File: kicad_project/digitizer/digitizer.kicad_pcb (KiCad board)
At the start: 2 copper layers, 96 x 74 mm, 63 parts, among them IC201 MAX3059ASA+T UPSTREAM, IC202 MAX6035AAUR50+T, IC203 MAX3059ASA+T DOWNSTREAM, IC204 MAX6043BAUT33+T, IC301 ADS1234IPWR, J201 DT15-4P (UPSTREAM), J202 DT06-4S (DOWNSTREAM), J301 Load Cell 1, J302 Load Cell 2, J303 Load Cell 3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

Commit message: continued layout progress; connected JTAG connector and reset switch, among a few other changes
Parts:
- C303: moved to F.Cu
- C405, R407: moved to B.Cu
- moved R307 103.3 mm to (130.5, 104.6)
- moved R306 84.3 mm to (130.5, 102.5)
- moved R407 81.3 mm to (99.3, 81.3), turned to 90 degrees
- moved R406 74.6 mm to (107.5, 59.2)
- moved C405 66.8 mm to (102.5, 82.2)
- moved R405 62.6 mm to (103.6, 59.2), turned to 180 degrees
- moved R401 62.5 mm to (98.8, 55.0), turned to 90 degrees
- moved R402 60.8 mm to (99.7, 59.2), turned to 180 degrees
- moved J401 5.10 mm to (101.5, 54.8), turned to 0 degrees
- moved REF** 4.24 mm to (82.2, 115.0)
- moved C304 3.00 mm to (147.4, 113.5)
- moved C306 3.00 mm to (83.0, 105.3)
- moved C307 3.00 mm to (113.5, 114.0)
- moved J202 3.00 mm to (85.5, 63.8)
- moved J301 3.00 mm to (85.5, 87.7)
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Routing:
- net NRESET: track 0.00 -> 35.2 mm
- net GND: track 28.5 -> 33.8 mm, vias 3 -> 4
- net MCU_NRESET: track 0.00 -> 4.56 mm, vias 0 -> 1
- net Net-(IC301-Pad20): track 0.00 -> 4.23 mm
- net /MCU/TCLK: track 0.00 -> 4.00 mm
- net /MCU/TDI: track 0.00 -> 3.67 mm
- net Net-(IC301-Pad19): track 0.00 -> 3.63 mm
- net /ANALOG/load cell 2 - signal (-): track 12.5 -> 8.90 mm
- net /MCU/TDO: track 0.00 -> 3.41 mm
- net /ANALOG/load cell 1 - signal (-): track 41.3 -> 38.3 mm
- net /ANALOG/load cell 1 - signal (+): track 42.3 -> 39.3 mm
- net /MCU/TMS: track 0.00 -> 2.68 mm
- net Net-(C303-Pad2): track 6.68 -> 5.17 mm, vias 1 -> 0
- net /CANPWR/CANH_DOWNSTREAM: track 39.3 -> 38.0 mm
- net /ANALOG/load cell 3 - signal (-): track 29.7 -> 28.5 mm
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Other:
- board size 96 x 74 mm -> 93 x 71 mm

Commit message: more progress! CAN ICs are done, just the MCU Power decoupling is left
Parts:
- C202, C203: moved to B.Cu
- moved C202 114.0 mm to (105.2, 97.5), turned to -90 degrees
- moved C203 107.7 mm to (95.5, 97.5), turned to -90 degrees
- moved R202 2.44 mm to (99.2, 93.3)
- moved C304 2.44 mm to (149.8, 114.0)
- moved J303 2.22 mm to (132.2, 111.5)
- moved IC203 2.20 mm to (95.5, 97.5)
- moved C307 1.54 mm to (112.0, 114.0)
- moved J302 1.50 mm to (94.5, 111.5)
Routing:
- net /CANPWR/CANL_UPSTREAM: track 0.00 -> 65.3 mm, vias 0 -> 2
- net /CANPWR/CANH_UPSTREAM: track 0.00 -> 61.6 mm, vias 0 -> 1
- net CAN_DOWN_RX: track 0.00 -> 44.0 mm, vias 0 -> 2
- net CAN_DOWN_TX: track 0.00 -> 41.9 mm, vias 0 -> 2
- net CAN_UP_RX: track 0.00 -> 38.3 mm, vias 0 -> 2
- net /MCU/TDO: track 3.41 -> 38.4 mm, vias 0 -> 2
- net CAN_UP_TX: track 0.00 -> 33.9 mm, vias 0 -> 2
- net /MCU/TDI: track 3.67 -> 34.1 mm
- net /MCU/TMS: track 2.68 -> 31.9 mm, vias 0 -> 2
- net /MCU/TCLK: track 4.00 -> 30.1 mm, vias 0 -> 2
- net 5V_CLEAN: track 0.00 -> 5.68 mm, vias 0 -> 2
- net GND: track 33.8 -> 39.4 mm, vias 4 -> 6
- net /ANALOG/load cell 3 - signal (+): track 23.6 -> 26.4 mm
- net /ANALOG/load cell 3 - signal (-): track 28.5 -> 31.1 mm
- net I2C_SCL: track 41.9 -> 43.5 mm
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
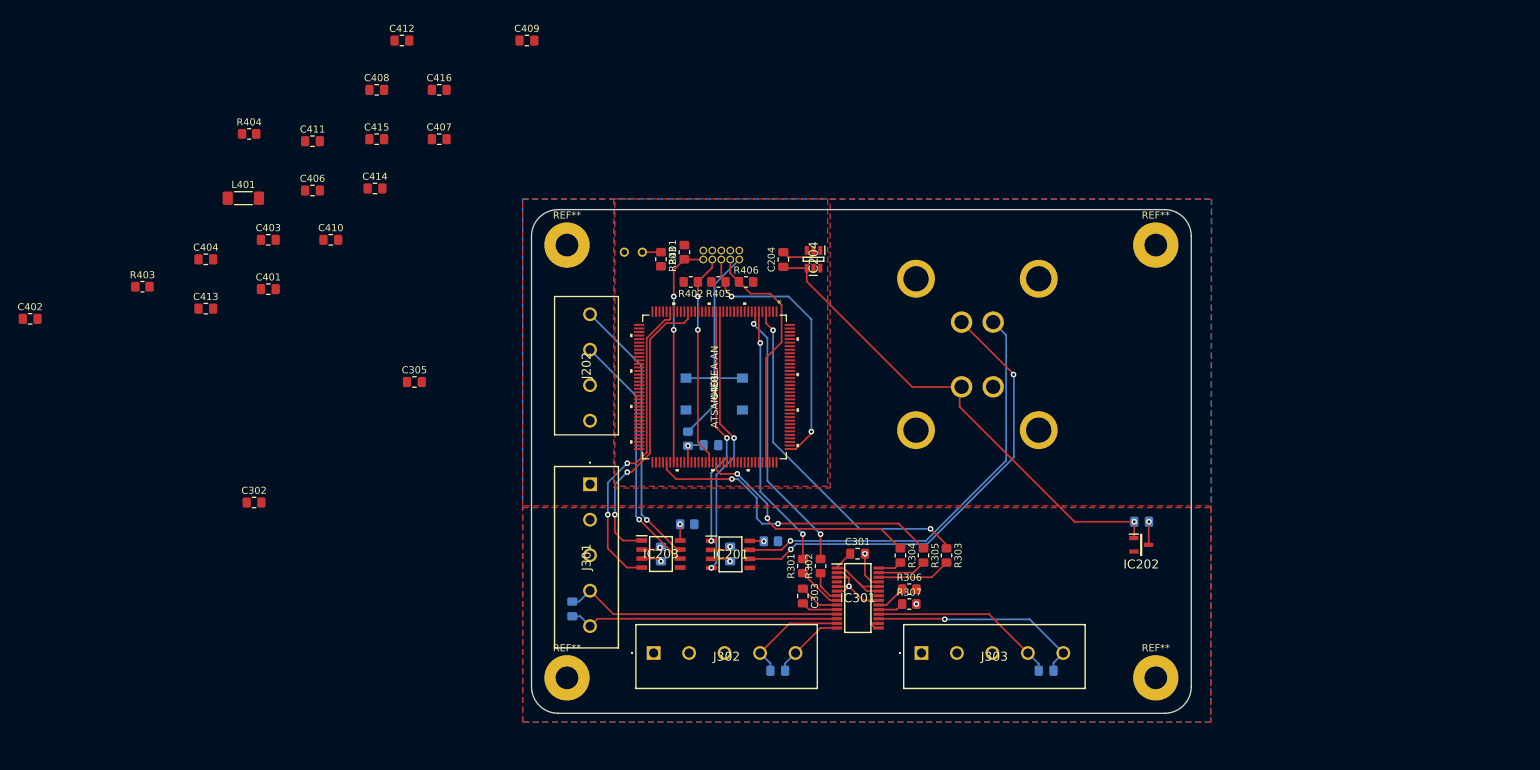
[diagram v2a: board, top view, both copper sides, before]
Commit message: modified the power planes so that the 12V plane routes above the 3V3 plane, not below it (thus making the space below the MCU less crowded). Also completed some further connections
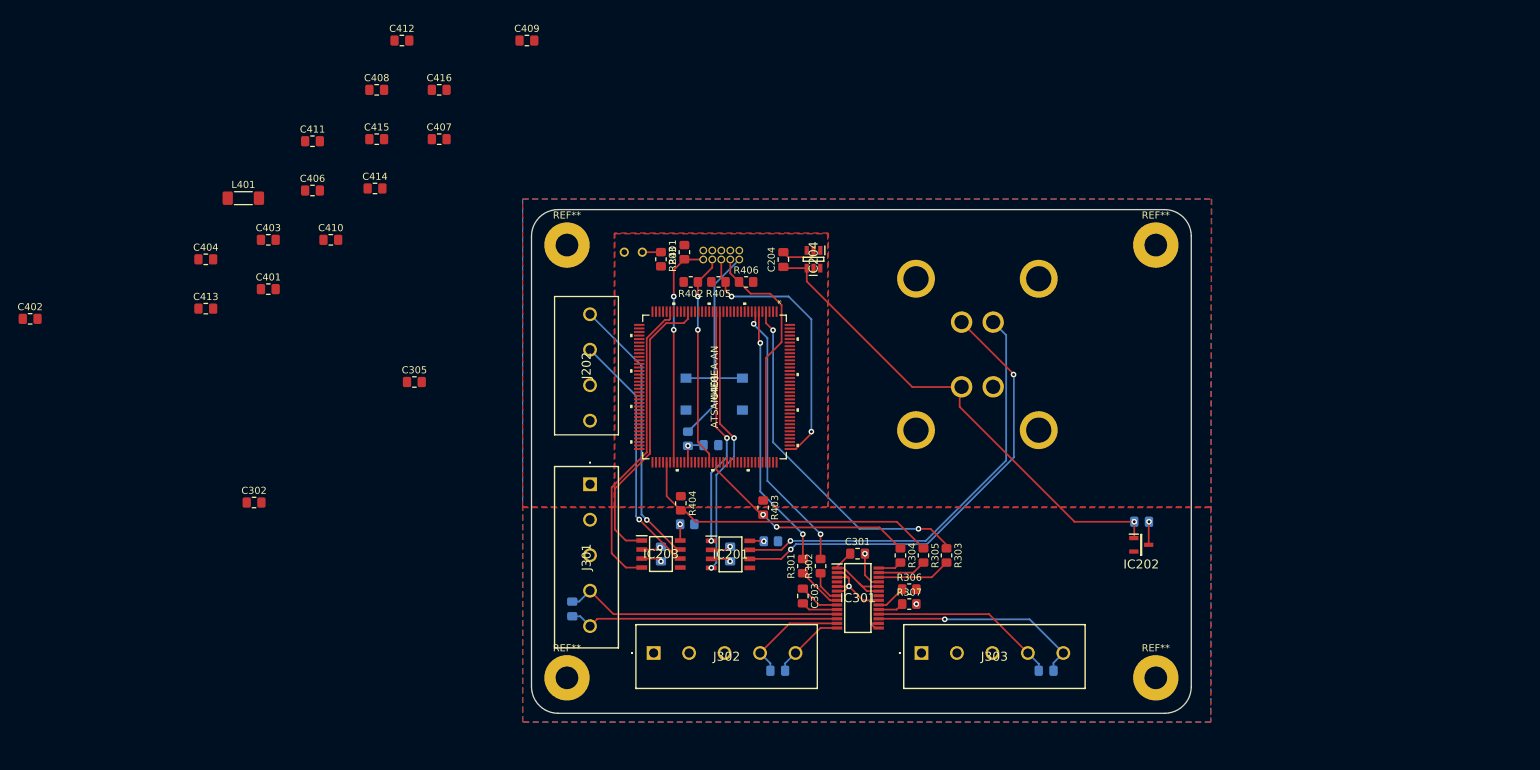
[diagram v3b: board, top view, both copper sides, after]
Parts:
- moved R403 92.9 mm to (109.9, 91.0), turned to -90 degrees
- moved R404 80.1 mm to (98.3, 90.4), turned to -90 degrees
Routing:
- net I2C_SDA: track 32.9 -> 31.8 mm
- net CAN_DOWN_RX: track 44.0 -> 42.9 mm, vias 2 -> 0
- net CAN_DOWN_TX: track 41.9 -> 41.3 mm, vias 2 -> 0
- net I2C_SCL: track 43.5 -> 44.0 mm, vias 2 -> 0

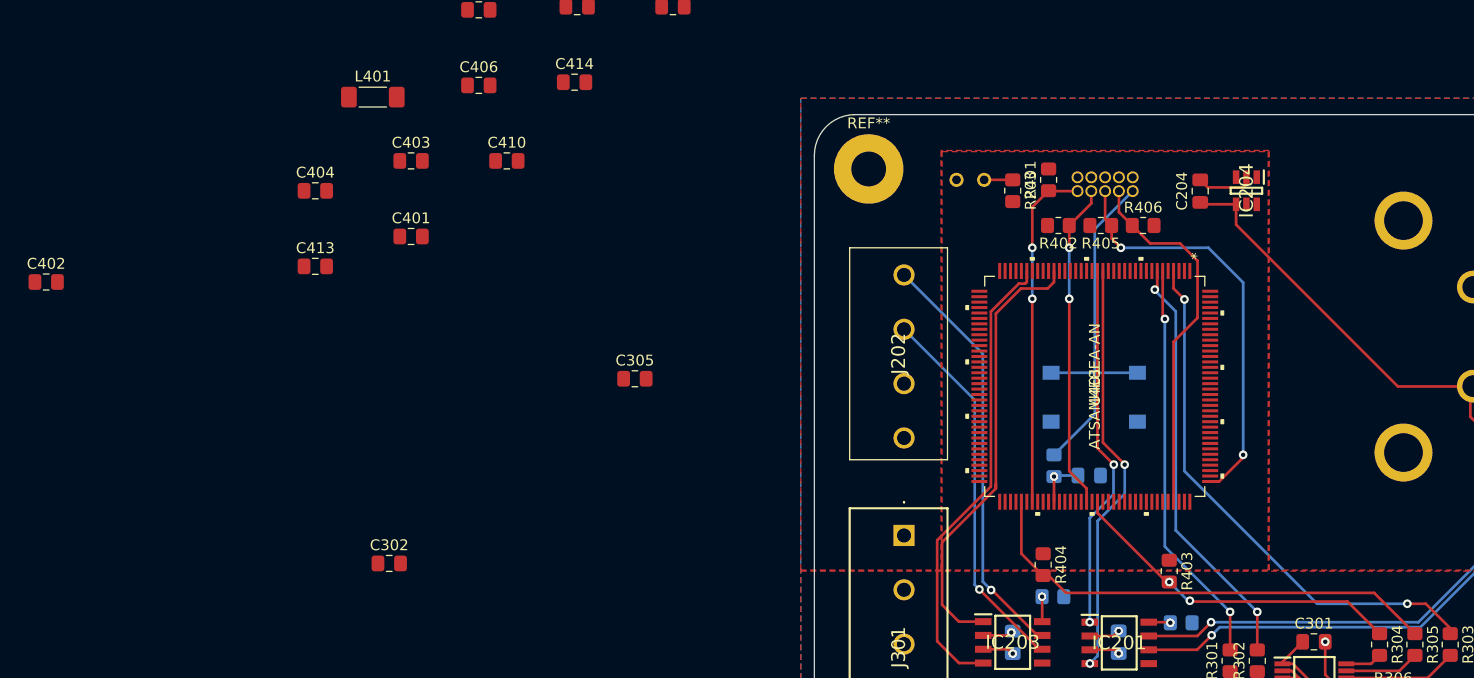
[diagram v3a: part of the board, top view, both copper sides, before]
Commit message: progress on connecting PWR/GND pins
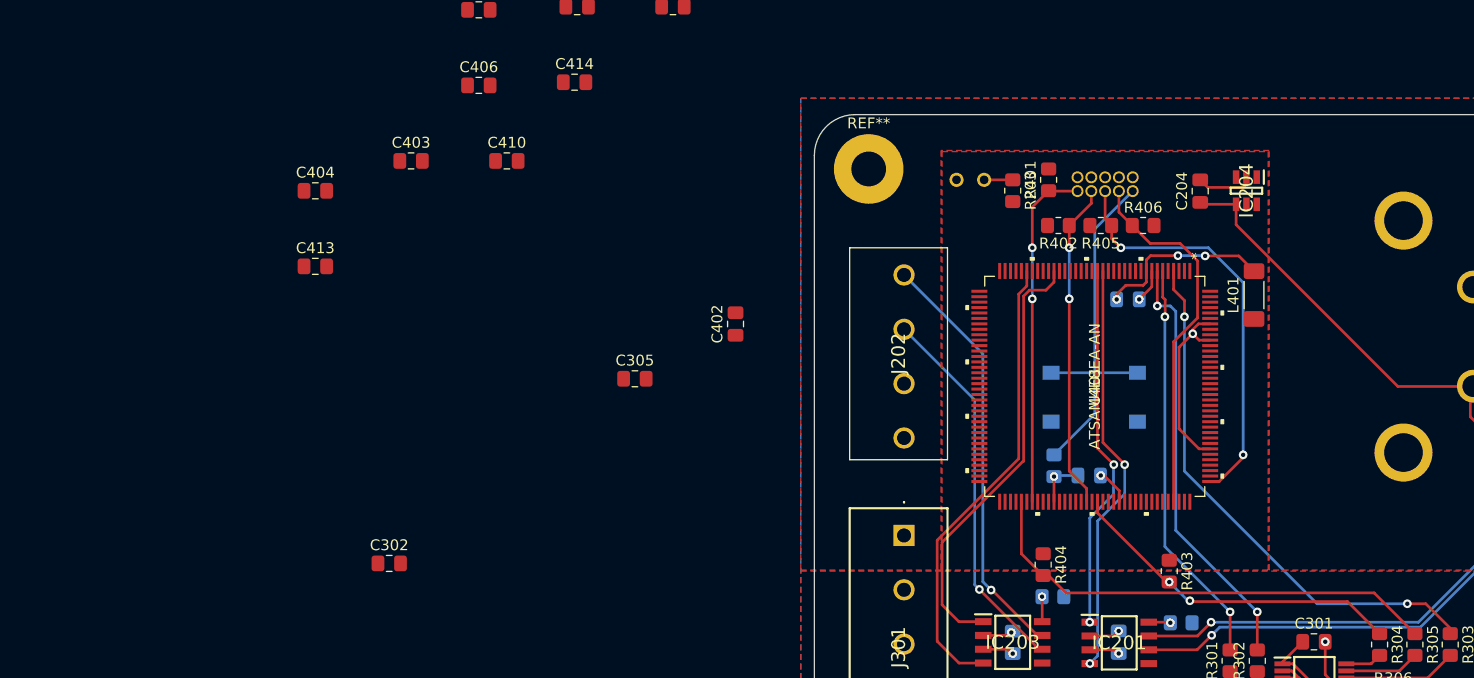
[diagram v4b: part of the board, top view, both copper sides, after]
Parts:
- C401: moved to B.Cu
- moved L401 83.1 mm to (117.7, 65.6), turned to 90 degrees
- moved C401 66.2 mm to (106.1, 66.0)
- moved C402 63.5 mm to (70.0, 68.3), turned to 90 degrees
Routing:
- net GND: track 39.4 -> 62.7 mm, vias 6 -> 9
- net Net-(C401-Pad1): track 0.00 -> 16.4 mm, vias 0 -> 3
- net CAN_DOWN_TX: track 41.3 -> 40.3 mm
- net ADC_MUX_1: track 38.9 -> 39.4 mm

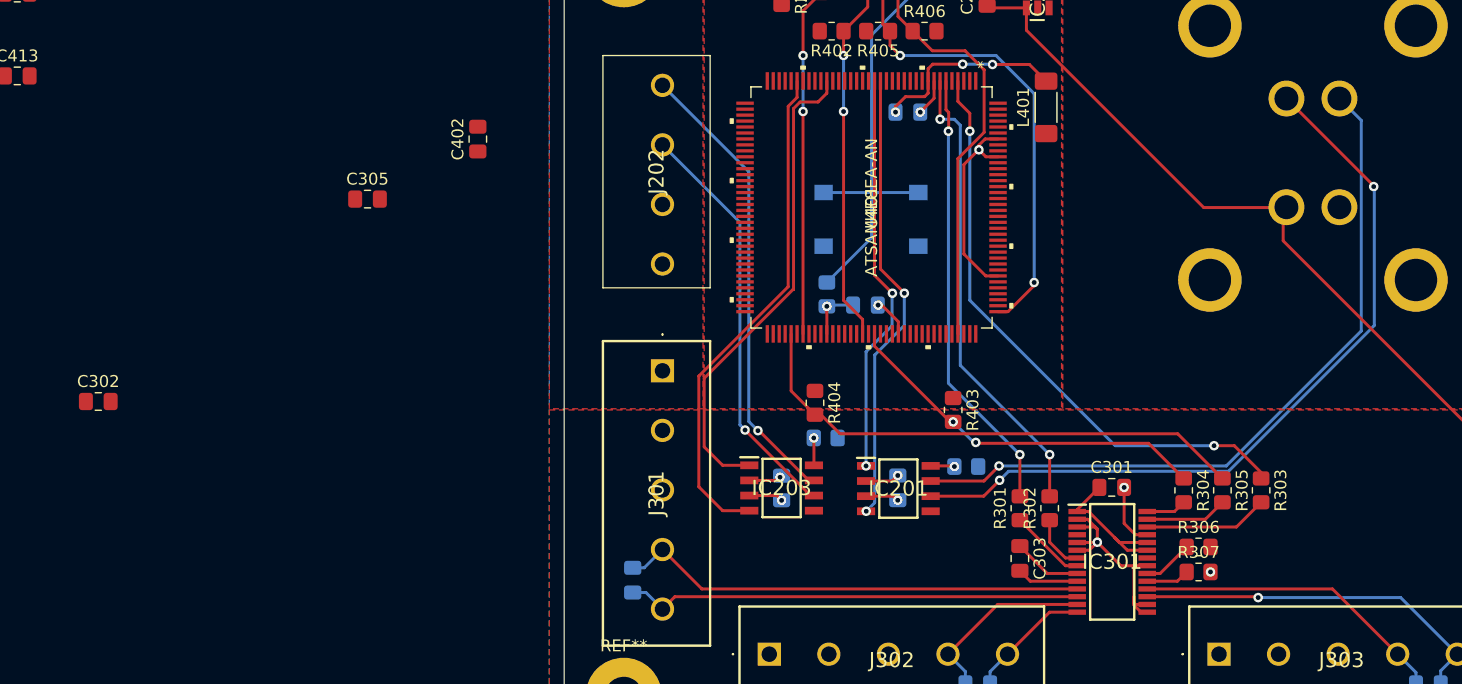
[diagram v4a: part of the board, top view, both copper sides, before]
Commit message: more progress; finished connecting all passives and components except for MCU power pins
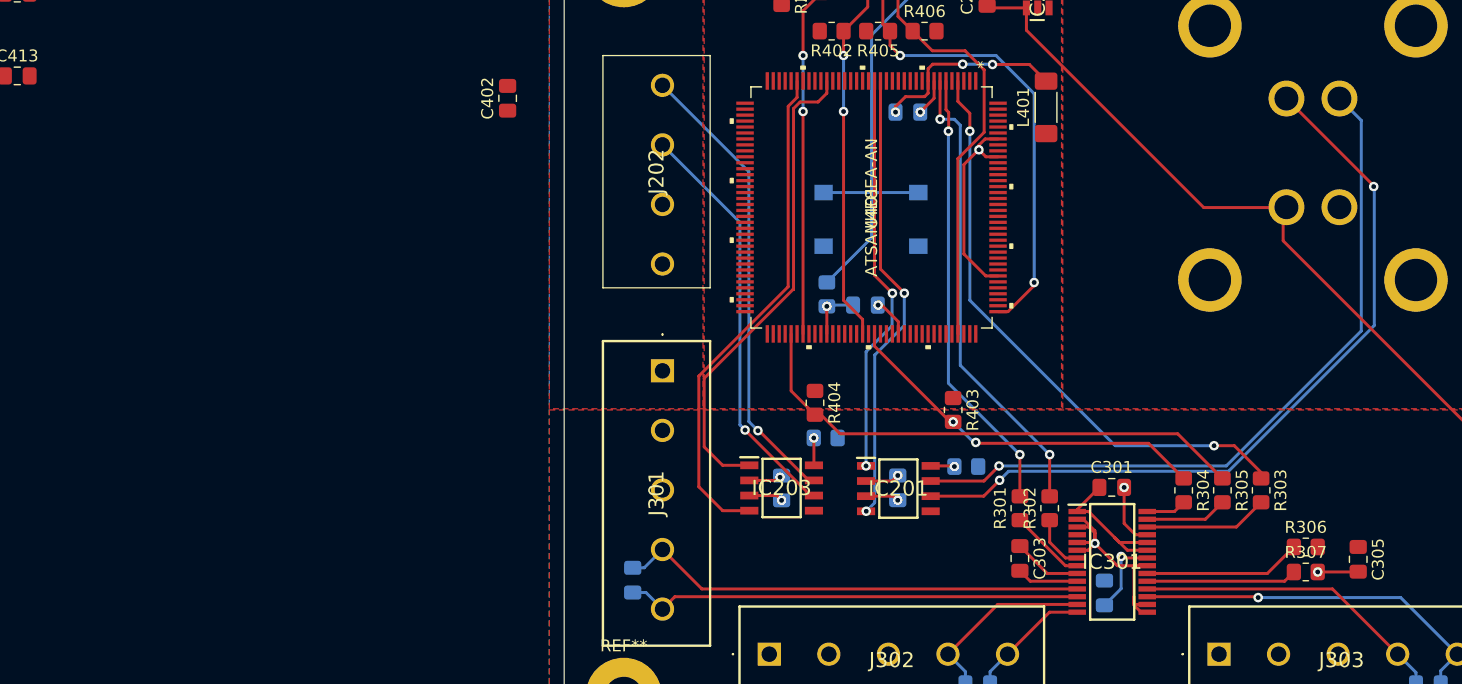
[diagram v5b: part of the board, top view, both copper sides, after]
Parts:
- C302: moved to B.Cu
- moved C305 88.5 mm to (143.9, 103.5), turned to -90 degrees
- moved C302 86.0 mm to (122.6, 106.4), turned to 90 degrees
- moved R306 9.00 mm to (139.5, 102.5)
- moved R307 9.00 mm to (139.5, 104.6)
- moved C402 4.24 mm to (72.5, 64.8)
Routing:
- net Net-(IC301-Pad20): track 4.23 -> 13.2 mm
- net Net-(IC301-Pad19): track 3.63 -> 12.6 mm
- net 5V_CLEAN: track 5.68 -> 12.6 mm, vias 2 -> 3
- net GND: track 62.7 -> 66.5 mm
